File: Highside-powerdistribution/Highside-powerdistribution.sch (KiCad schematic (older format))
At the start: 45 parts, among them J1 Screw_Terminal_01x02, J10 Screw_Terminal_01x02, J11 Screw_Terminal_01x02, J12 Screw_Terminal_01x02, J13 Screw_Terminal_01x02, J14 Conn_01x02, J15 Screw_Terminal_01x06, J2 Screw_Terminal_01x02, J3 Screw_Terminal_01x02, J4 Screw_Terminal_01x02, J5 Screw_Terminal_01x02, J6 Screw_Terminal_01x02, J7 Screw_Terminal_01x06, J8 Screw_Terminal_01x02, J9 Screw_Terminal_01x02, K1 DIPxx-1Axx-11x, K2 DIPxx-1Axx-11x, K3 DIPxx-1Axx-11x, K4 DIPxx-1Axx-11x, K5 DIPxx-1Axx-11x, K6 DIPxx-1Axx-11x, Q1 P-MOSFET, Q2 P-MOSFET, Q3 P-MOSFET, Q4 P-MOSFET, Q5 P-MOSFET, Q6 P-MOSFET

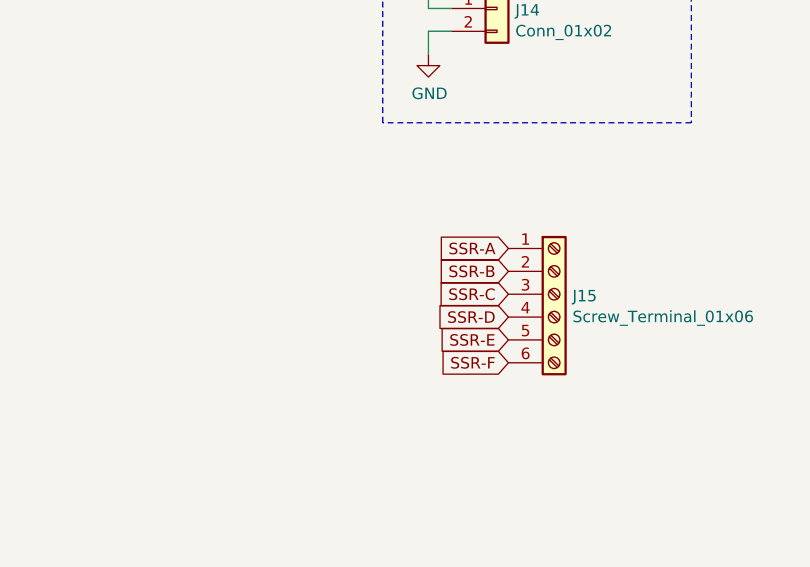
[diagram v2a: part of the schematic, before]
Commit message: Added 5x20 fuses on PCB
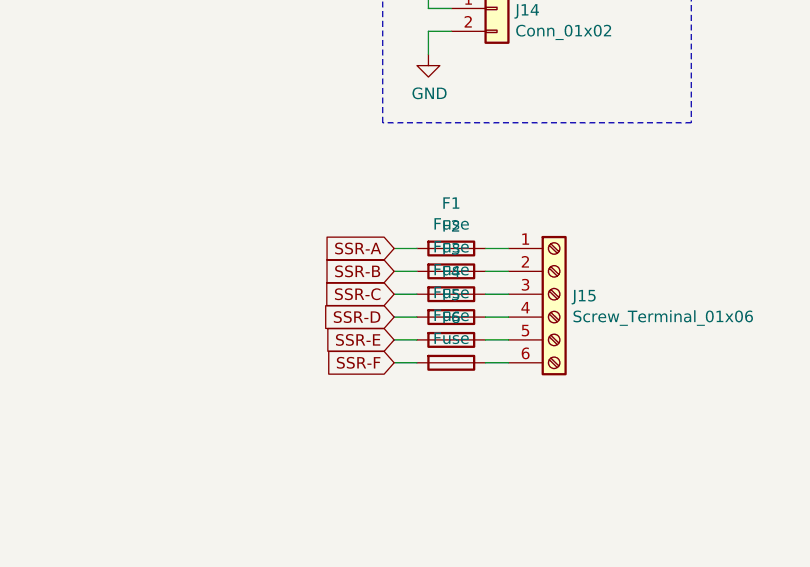
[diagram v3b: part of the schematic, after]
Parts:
- added F1, F2, F3, F4, F5, F6: Fuse, Highside-powerdistribution:PTF-15, symbol Device:Fuse
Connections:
- net SSR-A: now also F1.2; no longer J15.1 (Pin_1)
- net SSR-B: now also F2.2; no longer J15.2 (Pin_2)
- net SSR-C: now also F3.2; no longer J15.3 (Pin_3)
- net SSR-D: now also F4.2; no longer J15.4 (Pin_4)
- net SSR-E: now also F5.2; no longer J15.5 (Pin_5)
- net SSR-F: now also F6.2; no longer J15.6 (Pin_6)
- new net: F1.1, J15.1 (Pin_1)
- new net: F2.1, J15.2 (Pin_2)
- new net: F3.1, J15.3 (Pin_3)
- new net: F4.1, J15.4 (Pin_4)
- new net: F5.1, J15.5 (Pin_5)
- new net: F6.1, J15.6 (Pin_6)
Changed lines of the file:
@@
 	1    0    0    -1
 $EndComp
-Text GLabel 9100 4250 0    50   Input ~ 0
+Text GLabel 8600 4250 0    50   Input ~ 0
 SSR-A
-Text GLabel 9100 4350 0    50   Input ~ 0
+Text GLabel 8600 4350 0    50   Input ~ 0
 SSR-B
-Text GLabel 9100 4450 0    50   Input ~ 0
+Text GLabel 8600 4450 0    50   Input ~ 0
 SSR-C
-Text GLabel 9100 4550 0    50   Input ~ 0
+Text GLabel 8600 4550 0    50   Input ~ 0
 SSR-D
-Text GLabel 9100 4650 0    50   Input ~ 0
+Text GLabel 8600 4650 0    50   Input ~ 0
 SSR-E
-Text GLabel 9100 4750 0    50   Input ~ 0
+Text GLabel 8600 4750 0    50   Input ~ 0
 SSR-F
 $Comp
@@
 Wire Wire Line
 	5600 7500 5600 7550
+$Comp
+L Device:Fuse F1
+U 1 1 5DD1C641
+P 8850 4250
+F 0 "F1" V 8653 4250 50  0000 C CNN
+F 1 "Fuse" V 8744 4250 50  0000 C CNN
+F 2 "Highside-powerdistribution:PTF-15" V 8780 4250 50  0001 C CNN
+F 3 "~" H 8850 4250 50  0001 C CNN
+	1    8850 4250
+	0    1    1    0
+$EndComp
+$Comp
+L Device:Fuse F2
+U 1 1 5DD1CD8A
+P 8850 4350
+F 0 "F2" V 8653 4350 50  0000 C CNN
+F 1 "Fuse" V 8744 4350 50  0000 C CNN
+F 2 "Highside-powerdistribution:PTF-15" V 8780 4350 50  0001 C CNN
+F 3 "~" H 8850 4350 50  0001 C CNN
+	1    8850 4350
+	0    1    1    0
+$EndComp
+$Comp
+L Device:Fuse F3
+U 1 1 5DD1D01B
+P 8850 4450
+F 0 "F3" V 8653 4450 50  0000 C CNN
+F 1 "Fuse" V 8744 4450 50  0000 C CNN
+F 2 "Highside-powerdistribution:PTF-15" V 8780 4450 50  0001 C CNN
+F 3 "~" H 8850 4450 50  0001 C CNN
+	1    8850 4450
+	0    1    1    0
+$EndComp
+$Comp
+L Device:Fuse F4
+U 1 1 5DD1D0B5
+P 8850 4550
+F 0 "F4" V 8653 4550 50  0000 C CNN
+F 1 "Fuse" V 8744 4550 50  0000 C CNN
+F 2 "Highside-powerdistribution:PTF-15" V 8780 4550 50  0001 C CNN
+F 3 "~" H 8850 4550 50  0001 C CNN
+	1    8850 4550
+	0    1    1    0
+$EndComp
+$Comp
+L Device:Fuse F5
+U 1 1 5DD1D14A
+P 8850 4650
+F 0 "F5" V 8653 4650 50  0000 C CNN
+F 1 "Fuse" V 8744 4650 50  0000 C CNN
+F 2 "Highside-powerdistribution:PTF-15" V 8780 4650 50  0001 C CNN
+F 3 "~" H 8850 4650 50  0001 C CNN
+	1    8850 4650
+	0    1    1    0
+$EndComp
+$Comp
+L Device:Fuse F6
+U 1 1 5DD1D1DF
+P 8850 4750
+F 0 "F6" V 8653 4750 50  0000 C CNN
+F 1 "Fuse" V 8744 4750 50  0000 C CNN
+F 2 "Highside-powerdistribution:PTF-15" V 8780 4750 50  0001 C CNN
+F 3 "~" H 8850 4750 50  0001 C CNN
+	1    8850 4750
+	0    1    1    0
+$EndComp
+Wire Wire Line
+	8600 4250 8700 4250
+Wire Wire Line
+	8700 4350 8600 4350
+Wire Wire Line
+	8600 4450 8700 4450
+Wire Wire Line
+	8700 4550 8600 4550
+Wire Wire Line
+	8600 4650 8700 4650
+Wire Wire Line
+	8700 4750 8600 4750
+Wire Wire Line
+	9100 4750 9000 4750
+Wire Wire Line
+	9000 4650 9100 4650
+Wire Wire Line
+	9100 4550 9000 4550
+Wire Wire Line
+	9000 4450 9100 4450
+Wire Wire Line
+	9100 4350 9000 4350
+Wire Wire Line
+	9000 4250 9100 4250
 $EndSCHEMATC

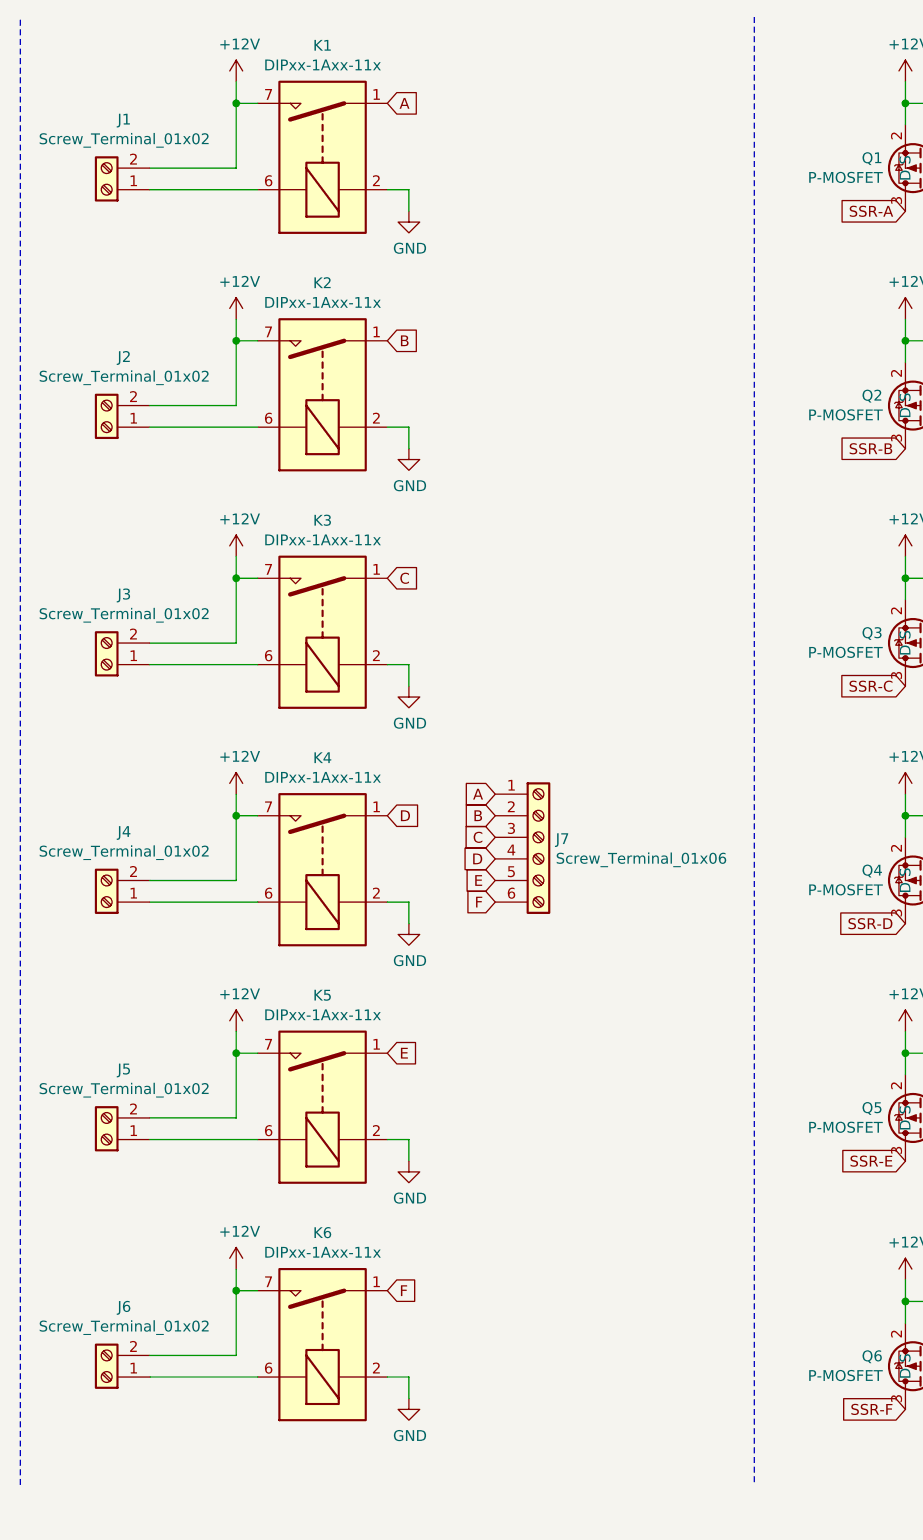
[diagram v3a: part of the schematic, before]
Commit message: Removed relay on schematic
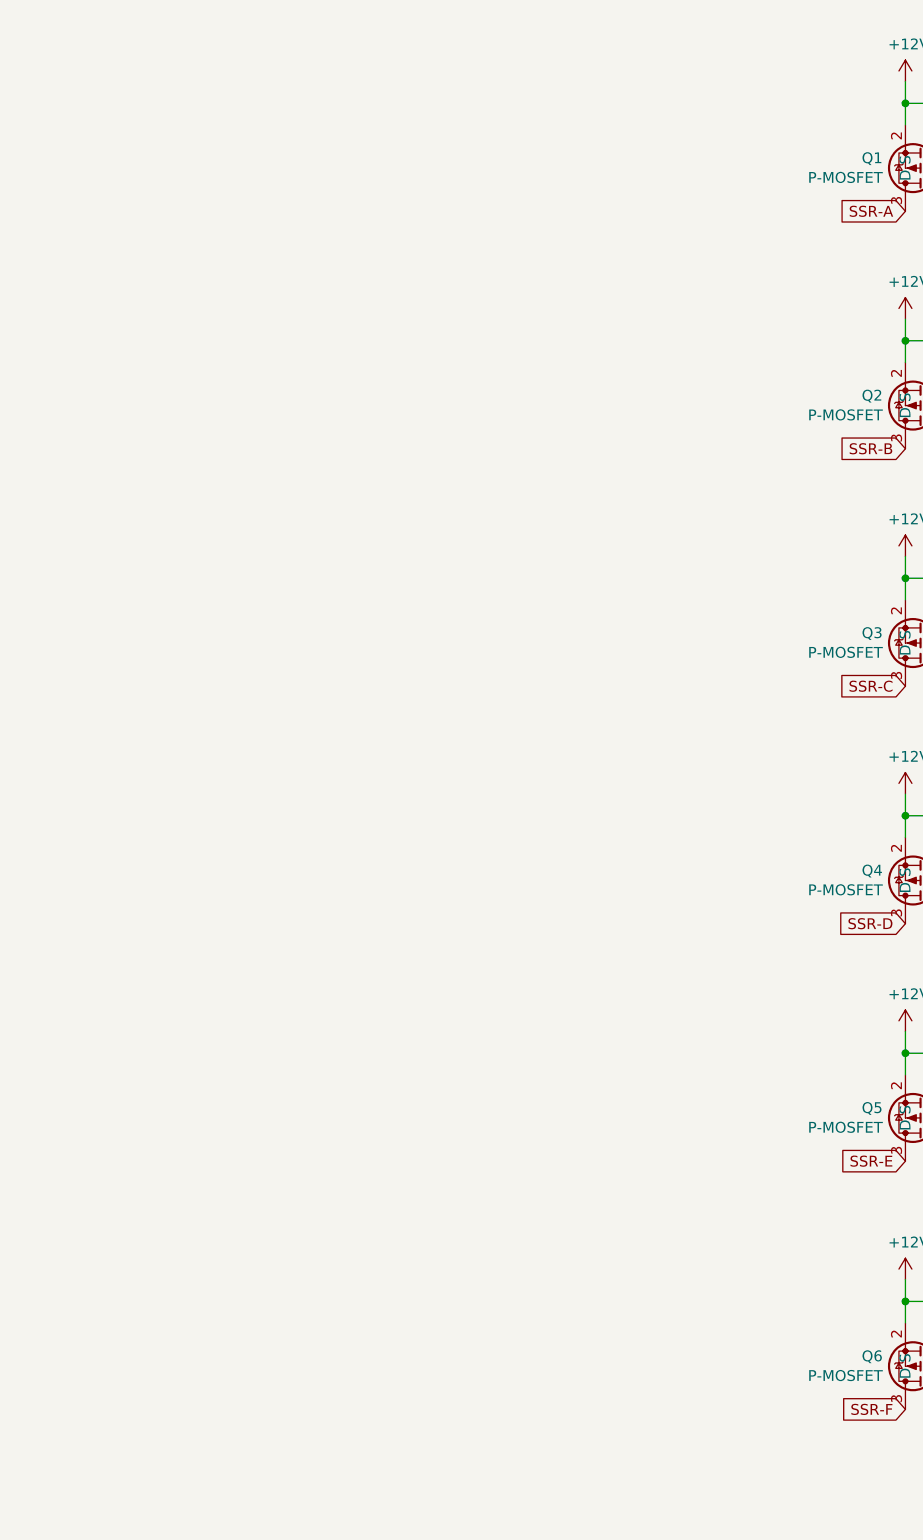
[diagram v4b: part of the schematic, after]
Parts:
- removed J1, J2, J3, J4, J5, J6: Screw_Terminal_01x02, Highside-powerdistribution:PTSA 1,5 2-3,5-Z, symbol Connector:Screw_Terminal_01x02
- removed J7: Screw_Terminal_01x06, symbol Connector:Screw_Terminal_01x06
- removed K1, K2, K3, K4, K5, K6: DIPxx-1Axx-11x, Relay_THT:Relay_StandexMeder_DIP_LowProfile, symbol Relay:DIPxx-1Axx-11x

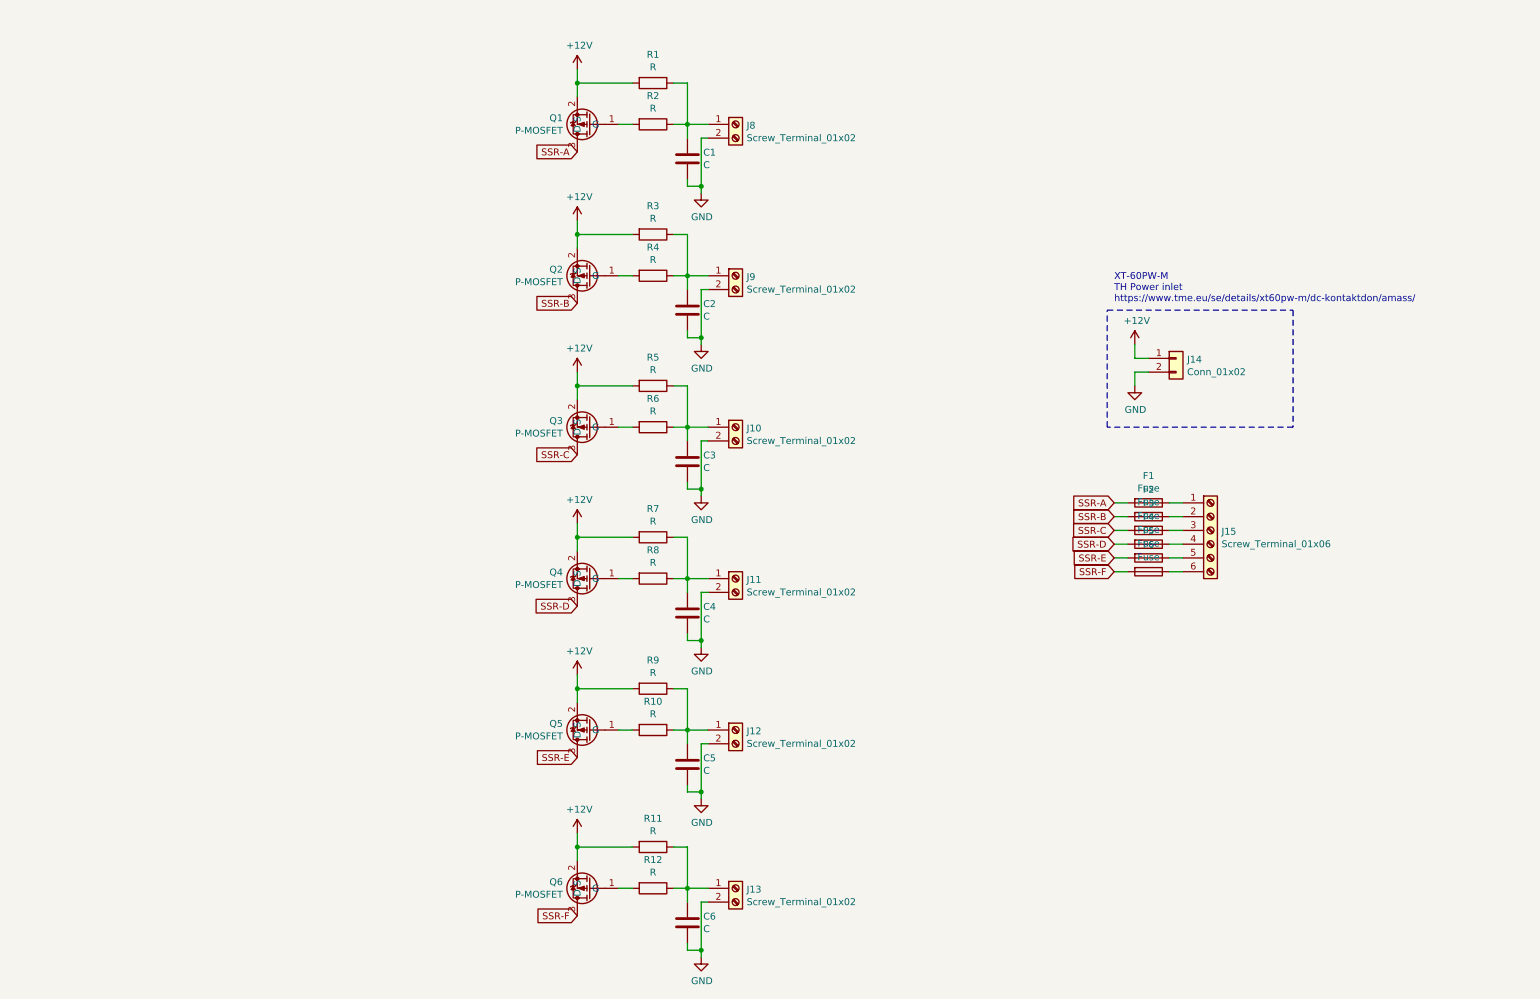
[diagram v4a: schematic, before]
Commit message: Added serie connector
To use one switch for multiple MOSFETs. Just a pinheader.
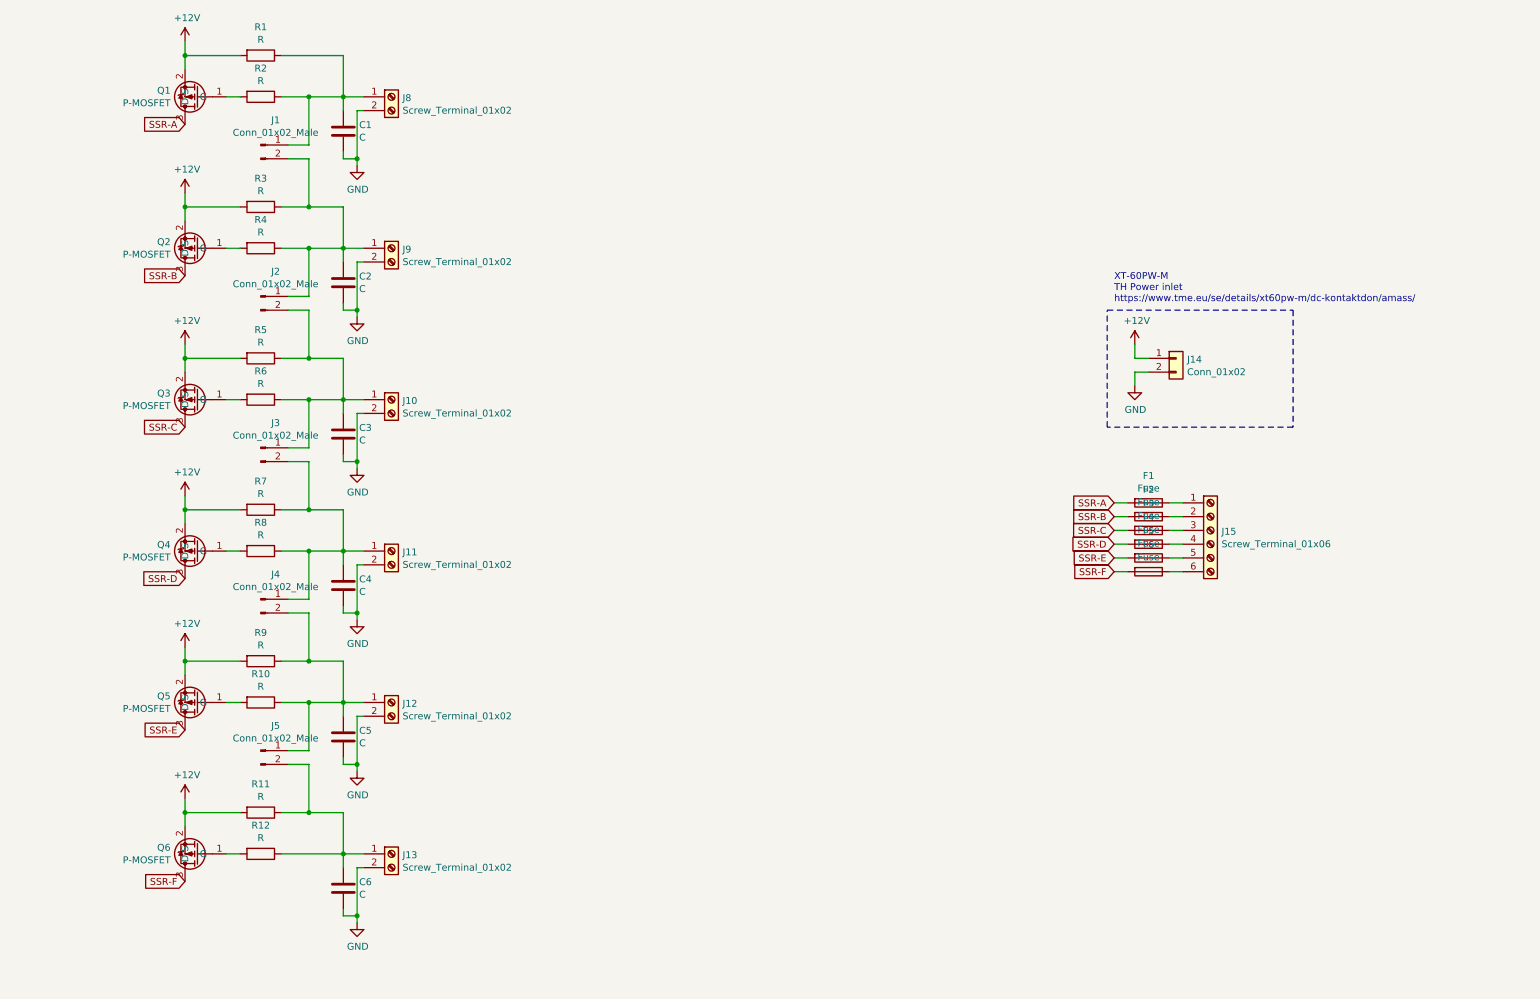
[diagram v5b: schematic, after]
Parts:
- added J1, J2, J3, J4, J5: Conn_01x02_Male, Connector_PinHeader_2.54mm:PinHeader_1x02_P2.54mm_Vertical, symbol Connector:Conn_01x02_Male
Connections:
- net at C1.1, J8.1 (Pin_1), R1.1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: now also J1.1 (Pin_1)
- net at C6.1, J13.1 (Pin_1), R11.1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: now also J5.2 (Pin_2)
- net at C2.1, J9.1 (Pin_1), R3.1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: now also J1.2 (Pin_2), J2.1 (Pin_1)
- net at C3.1, J10.1 (Pin_1), R5.1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: now also J2.2 (Pin_2), J3.1 (Pin_1)
- net at C4.1, J11.1 (Pin_1), R7.1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: now also J3.2 (Pin_2), J4.1 (Pin_1)
- net at C5.1, J12.1 (Pin_1), R10.1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: now also J4.2 (Pin_2), J5.1 (Pin_1)
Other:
- moved on the sheet: C1, C2, C3, C4, C5, C6, J10, J11, J12, J13, J8, J9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
